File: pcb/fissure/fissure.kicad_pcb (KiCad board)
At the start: 2 copper layers, 213.5 x 98.2 mm, 64 parts, among them J1 Conn_01x04_Female, J2 USB_C_Receptacle_USB2.0, J3 Conn_01x06, J4 Conn_01x06, J5 OLED, J6 Conn_01x06, J7 Conn_01x06, K1 KEY, K10 KEY, K11 KEY, K12 KEY, K13 KEY, K14 KEY, K15 KEY, K16 KEY, K17 KEY, K18 KEY, K19 KEY, K2 KEY, K20 KEY, K3 KEY, K4 KEY, K5 KEY, K6 KEY, K7 KEY, K8 KEY, K9 KEY, Q1 AO3401A, Q2 AO3401A, SW1 SW_Push, SW2 SW_Push, SW3 SW_SPDT, SW4 SW_SPDT, U1 Holyiot_18010, U2 MT25QL128ABA1ESE, U3 LTC4054ES5-4.2, U4 MCP1700-3302E_SOT23

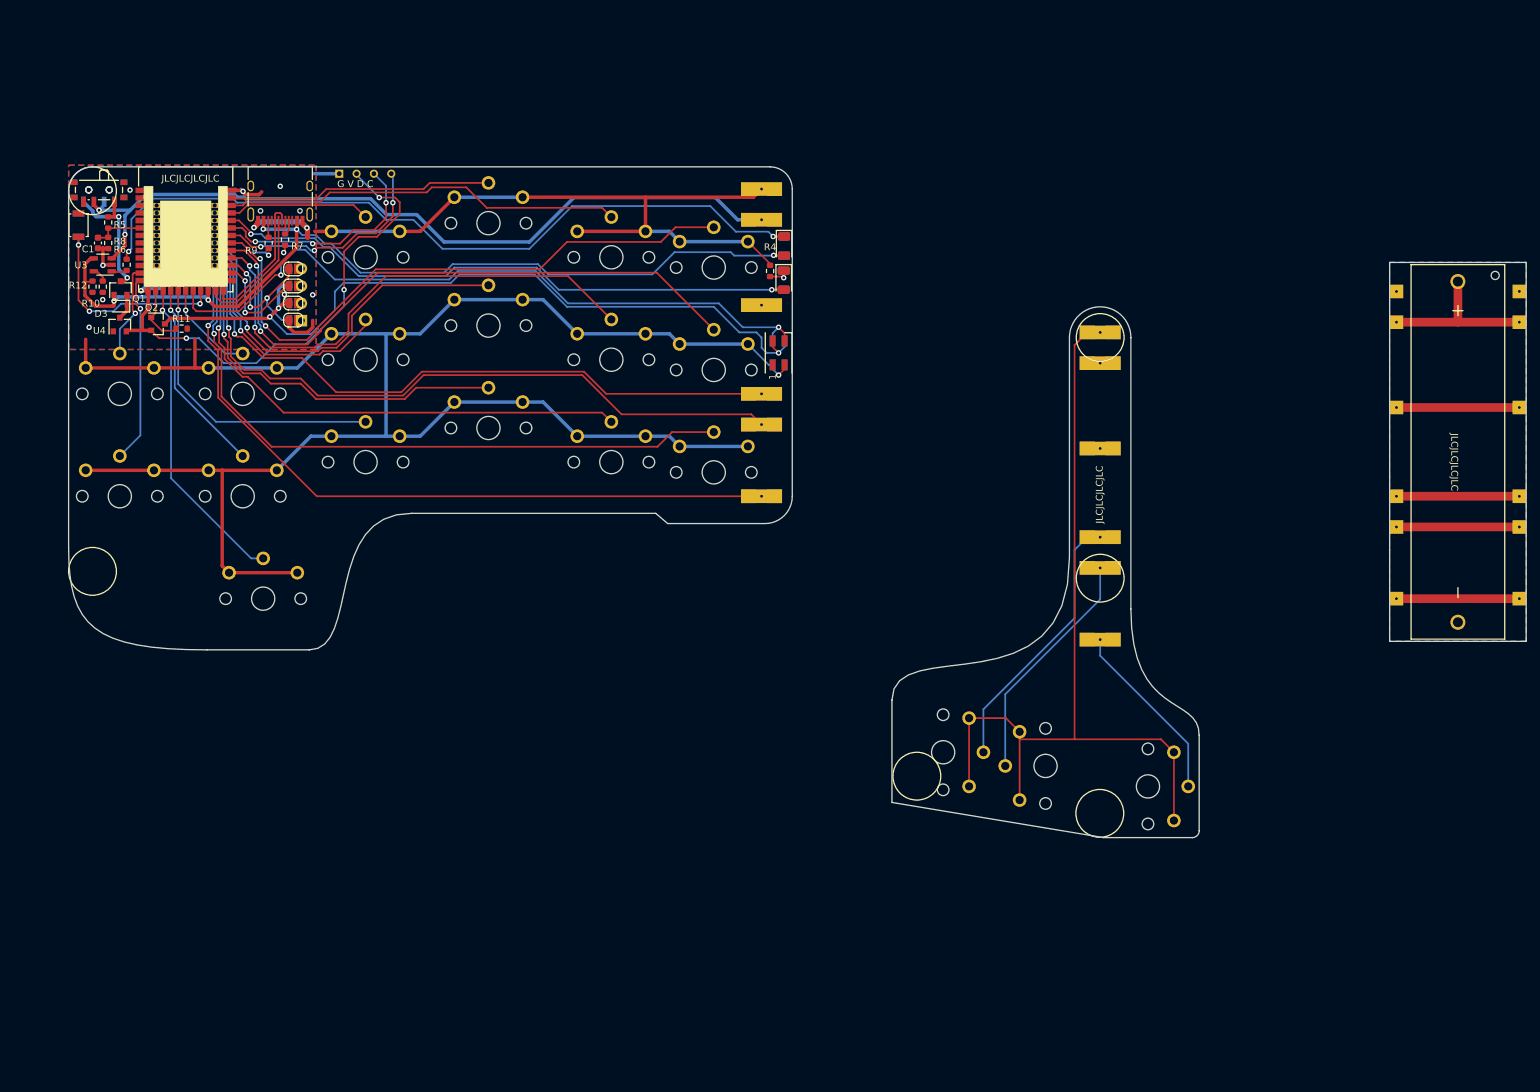
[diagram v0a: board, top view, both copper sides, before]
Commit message: stagger update
- middle 2 mm up
- outer index flat with home
- narrower pinky columns
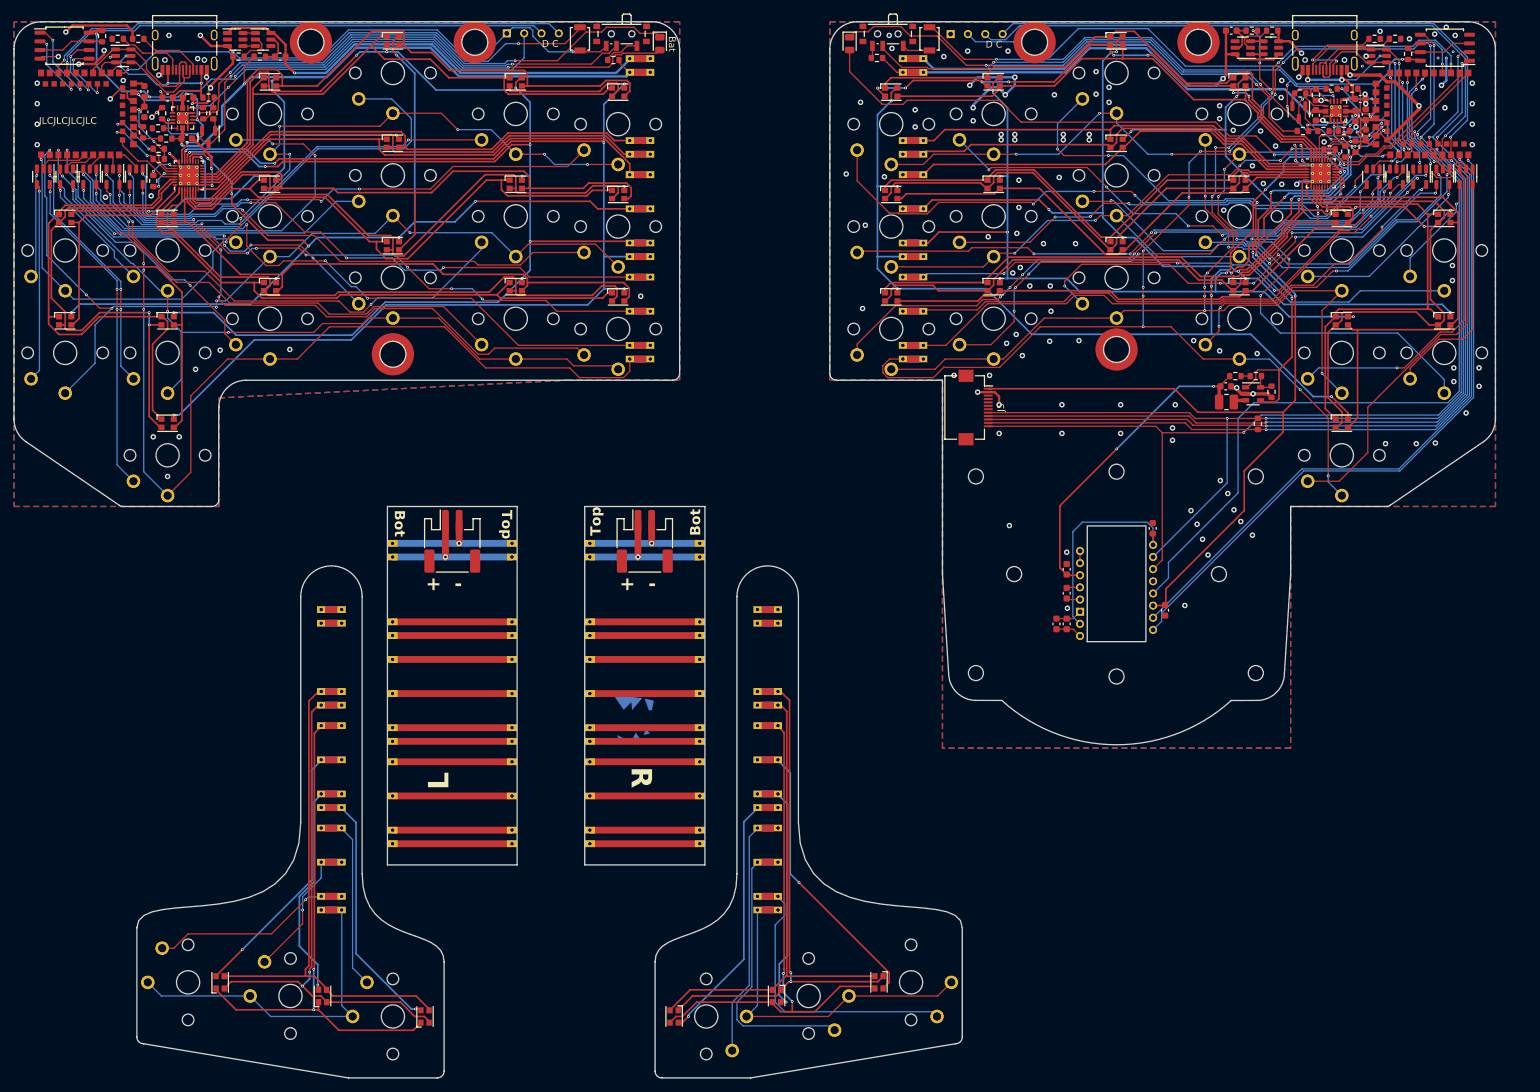
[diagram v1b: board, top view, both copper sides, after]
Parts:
- removed D41, D42: SK6812MINI, LED_SMD:LED_SK6812MINI_PLCC4_3.5x3.5mm_P1.75mm
- removed JP1, JP2, JP3, JP4, JP5, JP6, JP7, JP8: SolderJumper_2_Open, Jumper:SolderJumper-2_P1.3mm_Open_RoundedPad1.0x1.5mm
- added ?: , soldered-nuts:M2, F.Cu at (191.5, 38.0)
- added ?: , soldered-nuts:M2, F.Cu at (167.5, 38.0)
- added ?: , soldered-nuts:M2, F.Cu at (73.5, 83.7)
- added ?: , soldered-nuts:M2, F.Cu at (61.5, 38.0)
- added ?: , soldered-nuts:M2, F.Cu at (179.5, 83.0)
- added ?: , soldered-nuts:M2, F.Cu at (85.5, 38.0)
- added BT2: Battery_Cell, Connector_JST:JST_PH_S2B-PH-SM4-TB_1x02-1MP_P2.00mm_Horizontal, F.Cu at (110.4, 111.1)
- added C10: 10uF, Capacitor_SMD:C_0603_1608Metric, F.Cu at (170.7, 123.2)
- added C11: 10nF, Capacitor_SMD:C_0603_1608Metric, F.Cu at (172.2, 123.2)
- added C12: 10uF, Capacitor_SMD:C_0603_1608Metric, F.Cu at (195.5, 88.4)
- added C13: 4.7uF, Capacitor_SMD:C_0603_1608Metric, F.Cu at (215.2, 46.3)
- added C14: 4.7uF, Capacitor_SMD:C_0603_1608Metric, F.Cu at (214.5, 48.8)
- added C15: 4.7uF, Capacitor_SMD:C_0603_1608Metric, F.Cu at (208.7, 48.7)
- added C16: 0.1uF, Capacitor_SMD:C_0603_1608Metric, F.Cu at (57.0, 40.1)
- added C17: 0.1uF, Capacitor_SMD:C_0603_1608Metric, F.Cu at (196.3, 36.3)
- added C2: 4.7uF, Capacitor_SMD:C_0603_1608Metric, F.Cu at (40.5, 46.1)
- added C3: 4.7uF, Capacitor_SMD:C_0603_1608Metric, F.Cu at (43.5, 46.1)
- added C4: 4.7uF, Capacitor_SMD:C_0603_1608Metric, F.Cu at (43.3, 52.1)
- added C5: 4.7uF, Capacitor_SMD:C_0603_1608Metric, F.Cu at (216.0, 48.6)
- added C6: 100nF, Capacitor_SMD:C_0603_1608Metric, F.Cu at (186.6, 121.2)
- added C7: 100nF, Capacitor_SMD:C_0603_1608Metric, F.Cu at (172.2, 115.2)
- added C8: 100nF, Capacitor_SMD:C_0603_1608Metric, F.Cu at (172.2, 118.7)
- added C9: 10nF, Capacitor_SMD:C_0603_1608Metric, F.Cu at (184.8, 109.2)
- added D10: ~, Package_TO_SOT_SMD:SOT-23-5, F.Cu at (217.1, 57.7)
- added D11: ~, Package_TO_SOT_SMD:SOT-23-5, F.Cu at (230.7, 57.7)
- added D12: ~, Package_TO_SOT_SMD:SOT-23-5, F.Cu at (227.3, 57.7)
- added D6: ~, Package_TO_SOT_SMD:SOT-23-5, F.Cu at (32.5, 57.7)
- added D7: ~, Package_TO_SOT_SMD:SOT-23-5, F.Cu at (35.9, 57.7)
- added D8: ~, Package_TO_SOT_SMD:SOT-23-5, F.Cu at (223.9, 57.7)
- added D9: ~, Package_TO_SOT_SMD:SOT-23-5, F.Cu at (220.5, 57.7)
- added G***: LOGO, LOGO, B.Cu at (110.6, 136.0)
- added J11: Conn_01x12_Socket, fissure:bridge, B.Cu at (119.2, 130.1)
- added J12: Conn_01x12_Pin, fissure:bridge-conn, B.Cu at (149.7, 65.0)
- added J16: Conn_01x12_Pin, fissure:bridge-conn, F.Cu at (128.4, 145.7)
- added J17: Conn_01x12_Socket, fissure:bridge, F.Cu at (101.6, 130.1)
- added J8: USB_C_Receptacle_USB2.0, Connector_USB:USB_C_Receptacle_HRO_TYPE-C-31-M-12, F.Cu at (210.0, 38.0)
- added J9: debug-port, misc:debug-port-single-side, F.Cu at (159.0, 36.8)
- added K21: diode-choc, pg1350:pg1350-SR, F.Cu at (146.5, 50.0)
- added K22: diode-choc, pg1350:pg1350-SL, F.Cu at (161.5, 48.5)
- added K23: diode-choc, pg1350:pg1350-S, F.Cu at (179.5, 42.5)
- added K24: diode-choc, pg1350:pg1350-SR, F.Cu at (197.5, 48.5)
- added K25: diode-choc, pg1350:pg1350-SN, F.Cu at (212.5, 68.5)
- added K26: diode-choc, pg1350:pg1350-SR, F.Cu at (146.5, 65.0)
- added K27: diode-choc, pg1350:pg1350-SL, F.Cu at (161.5, 63.5)
- added K28: diode-choc, pg1350:pg1350-S, F.Cu at (179.5, 57.5)
- added K29: diode-choc, pg1350:pg1350-SR, F.Cu at (197.5, 63.5)
- added K30: diode-choc, pg1350:pg1350-SN, F.Cu at (212.5, 83.5)
- added K31: diode-choc, pg1350:pg1350-SR, F.Cu at (146.5, 80.0)
- added K32: diode-choc, pg1350:pg1350-SL, F.Cu at (161.5, 78.5)
- added K33: diode-choc, pg1350:pg1350-S, F.Cu at (179.5, 72.5)
- added K34: diode-choc, pg1350:pg1350-SR, F.Cu at (197.5, 78.5)
- added K35: diode-choc, pg1350:pg1350-SN, F.Cu at (212.5, 98.5)
- added K36: diode-choc, pg1350:pg1350-SN, F.Cu at (227.5, 68.5)
- added K37: diode-choc, pg1350:pg1350-SN, F.Cu at (227.5, 83.5)
- added K38: diode-choc, pg1350:pg1350-S, F.Cu at (119.4, 180.7)
- added K39: diode-choc, pg1350:pg1350-S, F.Cu at (134.4, 177.7)
- added K40: diode-choc, pg1350:pg1350-S, F.Cu at (149.4, 175.7)
- added L1: 10uH, Inductor_SMD:L_0603_1608Metric, F.Cu at (216.0, 51.6)
- added L2: 2.2uH, Inductor_SMD:L_1008_2520Metric, F.Cu at (195.6, 90.7)
- added L3: 10uH, Inductor_SMD:L_0603_1608Metric, F.Cu at (37.1, 45.2)
- added LED1: LED_BGRA, LED_SMD:LED_ASMB-KTF0-0A306, F.Cu at (40.5, 63.8)
- added LED10: LED_BGRA, LED_SMD:LED_ASMB-KTF0-0A306, F.Cu at (106.5, 60.3)
- added LED11: LED_BGRA, LED_SMD:LED_ASMB-KTF0-0A306, F.Cu at (40.5, 93.8)
- added LED12: LED_BGRA, LED_SMD:LED_ASMB-KTF0-0A306, F.Cu at (55.5, 73.8)
- added LED13: LED_BGRA, LED_SMD:LED_ASMB-KTF0-0A306, F.Cu at (73.5, 67.8)
- added LED14: LED_BGRA, LED_SMD:LED_ASMB-KTF0-0A306, F.Cu at (91.5, 73.8)
- added LED15: LED_BGRA, LED_SMD:LED_ASMB-KTF0-0A306, F.Cu at (106.5, 75.3)
- added LED16: LED_BGRA, LED_SMD:LED_ASMB-KTF0-0A306, F.Cu at (25.5, 63.8)
- added LED17: LED_BGRA, LED_SMD:LED_ASMB-KTF0-0A306, F.Cu at (25.5, 78.8)
- added LED18: LED_BGRA, LED_SMD:LED_ASMB-KTF0-0A306, F.Cu at (78.2, 180.7)
- added LED19: LED_BGRA, LED_SMD:LED_ASMB-KTF0-0A306, F.Cu at (63.2, 177.7)
- added LED2: LED_BGRA, LED_SMD:LED_ASMB-KTF0-0A306, F.Cu at (55.5, 43.8)
- added LED20: LED_BGRA, LED_SMD:LED_ASMB-KTF0-0A306, F.Cu at (48.2, 175.7)
- added LED21: LED_BGRA, LED_SMD:LED_ASMB-KTF0-0A306, F.Cu at (146.5, 45.3)
- added LED22: LED_BGRA, LED_SMD:LED_ASMB-KTF0-0A306, F.Cu at (161.5, 43.8)
- added LED23: LED_BGRA, LED_SMD:LED_ASMB-KTF0-0A306, F.Cu at (179.5, 37.8)
- added LED24: LED_BGRA, LED_SMD:LED_ASMB-KTF0-0A306, F.Cu at (197.5, 43.8)
- added LED25: LED_BGRA, LED_SMD:LED_ASMB-KTF0-0A306, F.Cu at (212.5, 63.8)
- added LED26: LED_BGRA, LED_SMD:LED_ASMB-KTF0-0A306, F.Cu at (146.5, 60.3)
- added LED27: LED_BGRA, LED_SMD:LED_ASMB-KTF0-0A306, F.Cu at (161.5, 58.8)
- added LED28: LED_BGRA, LED_SMD:LED_ASMB-KTF0-0A306, F.Cu at (179.5, 52.8)
- added LED29: LED_BGRA, LED_SMD:LED_ASMB-KTF0-0A306, F.Cu at (197.5, 58.8)
- added LED3: LED_BGRA, LED_SMD:LED_ASMB-KTF0-0A306, F.Cu at (73.5, 37.8)
- added LED30: LED_BGRA, LED_SMD:LED_ASMB-KTF0-0A306, F.Cu at (212.5, 78.8)
- added LED31: LED_BGRA, LED_SMD:LED_ASMB-KTF0-0A306, F.Cu at (146.5, 75.3)
- added LED32: LED_BGRA, LED_SMD:LED_ASMB-KTF0-0A306, F.Cu at (161.5, 73.8)
- added LED33: LED_BGRA, LED_SMD:LED_ASMB-KTF0-0A306, F.Cu at (179.5, 67.8)
- added LED34: LED_BGRA, LED_SMD:LED_ASMB-KTF0-0A306, F.Cu at (197.5, 73.8)
- added LED35: LED_BGRA, LED_SMD:LED_ASMB-KTF0-0A306, F.Cu at (212.5, 93.8)
- added LED36: LED_BGRA, LED_SMD:LED_ASMB-KTF0-0A306, F.Cu at (227.5, 78.8)
- added LED37: LED_BGRA, LED_SMD:LED_ASMB-KTF0-0A306, F.Cu at (227.5, 63.8)
- added LED38: LED_BGRA, LED_SMD:LED_ASMB-KTF0-0A306, F.Cu at (114.7, 180.7)
- added LED39: LED_BGRA, LED_SMD:LED_ASMB-KTF0-0A306, F.Cu at (129.7, 177.7)
- added LED4: LED_BGRA, LED_SMD:LED_ASMB-KTF0-0A306, F.Cu at (91.5, 43.8)
- added LED40: LED_BGRA, LED_SMD:LED_ASMB-KTF0-0A306, F.Cu at (144.7, 175.7)
- added LED5: LED_BGRA, LED_SMD:LED_ASMB-KTF0-0A306, F.Cu at (106.5, 45.3)
- added LED6: LED_BGRA, LED_SMD:LED_ASMB-KTF0-0A306, F.Cu at (40.5, 78.8)
- added LED7: LED_BGRA, LED_SMD:LED_ASMB-KTF0-0A306, F.Cu at (55.5, 58.8)
- added LED8: LED_BGRA, LED_SMD:LED_ASMB-KTF0-0A306, F.Cu at (73.5, 52.8)
- added LED9: LED_BGRA, LED_SMD:LED_ASMB-KTF0-0A306, F.Cu at (91.5, 58.8)
- added R1: 10k, Resistor_SMD:R_0603_1608Metric, F.Cu at (39.1, 50.6)
- added R13: 5.1k, Resistor_SMD:R_0603_1608Metric, F.Cu at (217.3, 37.5)
- added R14: 5.1k, Resistor_SMD:R_0603_1608Metric, F.Cu at (220.3, 37.5)
- added R15: 10k, Resistor_SMD:R_0603_1608Metric, F.Cu at (206.4, 45.5)
- added R16: 10k, Resistor_SMD:R_0603_1608Metric, F.Cu at (208.7, 45.7)
- added R17: 1k, Resistor_SMD:R_0603_1608Metric, F.Cu at (206.8, 51.0)
- added R18: 100k, Resistor_SMD:R_0603_1608Metric, F.Cu at (211.0, 44.8)
- added R19: 100k, Resistor_SMD:R_0603_1608Metric, F.Cu at (214.0, 44.8)
- added R2: 10k, Resistor_SMD:R_0603_1608Metric, F.Cu at (39.7, 48.4)
- added R20: 100k, Resistor_SMD:R_0603_1608Metric, F.Cu at (222.2, 39.7)
- added R21: 100k, Resistor_SMD:R_0603_1608Metric, F.Cu at (105.8, 40.6)
- added R22: 10k, Resistor_SMD:R_0603_1608Metric, F.Cu at (38.4, 58.3)
- added R23: 10k, Resistor_SMD:R_0603_1608Metric, F.Cu at (210.7, 53.7)
- added R24: 100k, Resistor_SMD:R_0603_1608Metric, F.Cu at (144.4, 40.3)
- added R25: 100k, Resistor_SMD:R_0603_1608Metric, F.Cu at (46.5, 46.1)
- added R26: 100k, Resistor_SMD:R_0603_1608Metric, F.Cu at (212.8, 51.0)
- added R27: 1k, Resistor_SMD:R_0603_1608Metric, F.Cu at (47.2, 48.4)
- added R28: 1k, Resistor_SMD:R_0603_1608Metric, F.Cu at (209.8, 51.0)
- added R29: 5.1k, Resistor_SMD:R_0603_1608Metric, F.Cu at (39.2, 53.6)
- added R30: 5.1k, Resistor_SMD:R_0603_1608Metric, F.Cu at (39.2, 55.1)
- added R31: 100, Resistor_SMD:R_0603_1608Metric, F.Cu at (54.0, 40.1)
- added R32: 100, Resistor_SMD:R_0603_1608Metric, F.Cu at (199.3, 36.3)
- added R33: 1k, Resistor_SMD:R_0603_1608Metric, F.Cu at (50.9, 40.1)
- added R34: 1k, Resistor_SMD:R_0603_1608Metric, F.Cu at (202.3, 36.3)
- added R35: 5.1k, Resistor_SMD:R_0603_1608Metric, F.Cu at (213.0, 54.0)
- added R36: 5.1k, Resistor_SMD:R_0603_1608Metric, F.Cu at (214.5, 53.3)
- added REF**: MountingHole_2.2mm_M2_DIN965, MountingHole:MountingHole_2.2mm_M2_DIN965, F.Cu at (194.5, 115.9)
- added REF**: MountingHole_2.2mm_M2_DIN965, MountingHole:MountingHole_2.2mm_M2_DIN965, F.Cu at (164.5, 115.9)
- added REF**: nothing, misc:nothing, F.Cu at (105.5, 84.5)
- added REF**: MountingHole_2.2mm_M2_DIN965, MountingHole:MountingHole_2.2mm_M2_DIN965, F.Cu at (179.5, 100.9)
- added REF**: MountingHole_2.2mm_M2_DIN965, MountingHole:MountingHole_2.2mm_M2_DIN965, F.Cu at (179.5, 130.9)
- added REF**: MountingHole_2.2mm_M2_DIN965, MountingHole:MountingHole_2.2mm_M2_DIN965, F.Cu at (158.9, 101.6)
- added REF**: embedded, misc:embedded, B.Cu at (84.0, 136.0)
- added REF**: crides-neg, misc:crides-neg, B.Cu at (84.0, 150.5)
- added REF**4: MountingHole_2.2mm_M2_DIN965, MountingHole:MountingHole_2.2mm_M2_DIN965, F.Cu at (199.9, 101.6)
- added REF**5: MountingHole_2.2mm_M2_DIN965, MountingHole:MountingHole_2.2mm_M2_DIN965, F.Cu at (158.9, 130.4)
- added REF**6: MountingHole_2.2mm_M2_DIN965, MountingHole:MountingHole_2.2mm_M2_DIN965, F.Cu at (199.9, 130.4)
- added U10: W25Q128JVS, Package_SO:SOIC-8_5.23x5.23mm_P1.27mm, F.Cu at (227.6, 38.8)
- added U11: DW01A, Package_TO_SOT_SMD:SOT-23-6, F.Cu at (54.5, 37.6)
- added U12: e73-2gm08s1c, mcu:e73-2g4m08s1c-shrunk, F.Cu at (27.0, 48.5)
- added U13: IS31FL3729, Package_DFN_QFN:QFN-32-1EP_4x4mm_P0.4mm_EP2.9x2.9mm_ThermalVias, F.Cu at (209.4, 57.2)
- added U14: DW01A, Package_TO_SOT_SMD:SOT-23-6, F.Cu at (198.0, 38.8)
- added U15: FS8205, Package_TO_SOT_SMD:SOT-23-6, F.Cu at (50.4, 37.6)
- added U16: FS8205, Package_TO_SOT_SMD:SOT-23-6, F.Cu at (202.1, 38.8)
- added U5: PMW3610, sensor:PMW3610, B.Cu at (179.5, 115.9)
- added U6: IS31FL3729, Package_DFN_QFN:QFN-32-1EP_4x4mm_P0.4mm_EP2.9x2.9mm_ThermalVias, F.Cu at (43.6, 57.5)
- added U7: SRV05-4, Package_TO_SOT_SMD:SOT-23-6, F.Cu at (217.9, 40.0)
- added U8: SRV05-4, Package_TO_SOT_SMD:SOT-23-6, F.Cu at (34.0, 40.0)
- added U9: BQ24075, Package_DFN_QFN:VQFN-16-1EP_3x3mm_P0.5mm_EP1.68x1.68mm_ThermalVias, F.Cu at (211.6, 48.1)
- BT1: footprint misc:BA1AAAPC -> Connector_JST:JST_PH_S2B-PH-SM4-TB_1x02-1MP_P2.00mm_Horizontal
- C1: value 10nF -> 4.7uF
- D1: value BLUE -> RED; footprint LED_SMD:LED_1206_3216Metric -> LED_SMD:LED_0805_2012Metric
- D2: footprint LED_SMD:LED_1206_3216Metric -> LED_SMD:LED_0805_2012Metric; moved to F.Cu
- D3: value 1N5819 -> ~; footprint Diode_SMD:D_SOD-323 -> Package_TO_SOT_SMD:SOT-23-5
- D4: value BLUE -> ~; footprint LED_SMD:LED_1206_3216Metric -> Package_TO_SOT_SMD:SOT-23-5; moved to F.Cu
- D5: value RED -> ~; footprint LED_SMD:LED_1206_3216Metric -> Package_TO_SOT_SMD:SOT-23-5
- J1: value Conn_01x04_Female -> debug-port; footprint fissure:debug-port -> misc:debug-port-single-side
- J3: value Conn_01x06 -> Conn_01x12_Pin; moved to B.Cu
- J4: value Conn_01x06 -> Conn_01x12_Pin; moved to F.Cu
- J5: value OLED -> cirque-trackpad; footprint misc:OLED -> Connector_FFC-FPC:Hirose_FH12-12S-0.5SH_1x12-1MP_P0.50mm_Horizontal; moved to F.Cu
- J6: value Conn_01x06 -> Conn_01x12_Socket
- J7: value Conn_01x06 -> Conn_01x12_Socket; moved to B.Cu
- K1, K11, K16, K17, K6: value KEY -> diode-choc; footprint pg1350:PG1350-reversible-no-diode-short -> pg1350:pg1350-SN
- K10, K15, K5: value KEY -> diode-choc; footprint pg1350:PG1350-reversible-no-diode-short-offcenter-outer -> pg1350:pg1350-SL
- K12, K2, K7: value KEY -> diode-choc; footprint pg1350:PG1350-reversible-no-diode-short -> pg1350:pg1350-SL
- K13, K18, K19, K20, K3, K8: value KEY -> diode-choc; footprint pg1350:PG1350-reversible-no-diode-short -> pg1350:pg1350-S
- K14, K4, K9: value KEY -> diode-choc; footprint pg1350:PG1350-reversible-no-diode-short-offcenter -> pg1350:pg1350-SR
- Q1, Q2: value AO3401A -> AO3400A
- R10: value 10k -> 100k
- R11: value 2M -> 100k
- R3: value 10k -> 100k; footprint Resistor_SMD:R_0805_2012Metric -> Resistor_SMD:R_0603_1608Metric; moved to F.Cu
- R4: value 1k -> 10k
- R5, R8: value 5.1M -> 100k
- SW2, SW3: moved to F.Cu
- U1: value Holyiot_18010 -> e73-2gm08s1c; footprint misc:Holyiot_18010 -> mcu:e73-2g4m08s1c-shrunk
- U2: value MT25QL128ABA1ESE -> W25Q128JVS; footprint Package_SO:SOP-8_5.28x5.23mm_P1.27mm -> Package_SO:SOIC-8_5.23x5.23mm_P1.27mm; moved to F.Cu
- U3: value LTC4054ES5-4.2 -> BQ24075; footprint Package_TO_SOT_SMD:TSOT-23-5 -> Package_DFN_QFN:VQFN-16-1EP_3x3mm_P0.5mm_EP1.68x1.68mm_ThermalVias
- U4: value MCP1700-3302E_SOT23 -> TLV62568DBV; footprint Package_TO_SOT_SMD:SOT-23 -> Package_TO_SOT_SMD:SOT-23-5
- moved U1 183.6 mm to (226.0, 48.5), turned to -90 degrees
- moved R12 173.4 mm to (202.2, 89.2), turned to 90 degrees
- moved Q2 169.9 mm to (206.2, 48.3), turned to -90 degrees
- moved R10 166.4 mm to (196.9, 86.9), turned to 0 degrees
- moved U4 166.3 mm to (199.5, 89.5), turned to 0 degrees
- moved R11 157.5 mm to (199.9, 86.9)
- moved J6 150.9 mm to (72.7, 130.1), turned to -90 degrees
- moved J7 150.0 mm to (91.7, 130.1), turned to -90 degrees
- moved BT1 147.9 mm to (82.2, 111.1), turned to 0 degrees
- moved SW2 127.6 mm to (152.1, 37.5), turned to -90 degrees
- moved J4 119.6 mm to (64.5, 145.7)
- moved SW3 117.8 mm to (146.0, 37.1), turned to 180 degrees
- moved K18 115.6 mm to (73.5, 180.7), turned to 90 degrees
- moved K19 115.6 mm to (58.5, 177.7)
- moved K20 115.6 mm to (43.5, 175.7), turned to 90 degrees
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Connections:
- BT1 pad 1: bridge_BAT -> Net-(BT1-+)
- BT1 pad 2: bridge_GND -> Net-(BT1--)
- C1 pad 1: BAT_MEAS -> L_3V3
- C1 pad 2: GND -> L_GND
- D1 pad 1: Net-(D1-Pad1) -> Net-(D1-K)
- D1 pad 2: BLUE -> L_VDDH
- D2 pad 1: Net-(D2-Pad1) -> Net-(D2-K)
- D2 pad 2: VBUS -> R_VDDH
- D3 pad 1: Net-(D3-Pad1) -> Net-(D3A-A)
- D3 pad 2: VBUS -> L_COL0
- D4 pad 1: Net-(D1-Pad1) -> Net-(D4A-A)
- D4 pad 2: BLUE -> L_COL1
- D5 pad 1: Net-(D2-Pad1) -> Net-(D5A-A)
- D5 pad 2: VBUS -> L_COL2
- J1 pad 1: GND -> L_GND
- J1 pad 2: VDD -> L_3V3
- J1 pad 3: SWC -> L_SWD
- J1 pad 4: SWD -> L_SWC
- J2 pad A1: GND -> L_GND
- J2 pad A12: GND -> L_GND
- J2 pad A4: VBUS -> L_VBUS
- J2 pad A6: D+ -> L_D+
- J2 pad A7: D- -> L_D-
- J2 pad A9: VBUS -> L_VBUS
- J2 pad B1: GND -> L_GND
- J2 pad B12: GND -> L_GND
- J2 pad B4: VBUS -> L_VBUS
- J2 pad B6: D+ -> L_D+
- J2 pad B7: D- -> L_D-
- J2 pad B9: VBUS -> L_VBUS
- J3 pad 1: GND -> L_ROW3
- J3 pad 2: BAT -> Net-(D5D-A)
- J3 pad 3: unconnected-(J3-Pad3) -> Net-(D6D-A)
- J3 pad 4: K20 -> Net-(D7D-A)
- J3 pad 5: K19 -> /thumb+led_l/A3
- J3 pad 6: K18 -> /thumb+led_l/A2
- J4 pad 1: thumb_GND -> Net-(J4-Pin_1)
- J4 pad 2: thumb_BAT -> Net-(J4-Pin_2)
- J4 pad 3: unconnected-(J4-Pad3) -> Net-(J4-Pin_3)
- J4 pad 4: thumb_K20 -> Net-(J4-Pin_4)
- J4 pad 5: thumb_K19 -> /thumb+led_l/T_A3
- J4 pad 6: thumb_K18 -> /thumb+led_l/T_A2
- J5 pad 1: Net-(J5-Pad1) -> R_3V3
- J5 pad 2: Net-(J5-Pad2) -> L_GND
- J5 pad 3: Net-(J5-Pad3) -> unconnected-(J5-SDA-Pad3)
- J5 pad 4: Net-(J5-Pad4) -> unconnected-(J5-SCL-Pad4)
- J6 pad 1: bridge_GND -> Net-(J6-Pin_1)
- J6 pad 2: bridge_BAT -> Net-(J6-Pin_2)
- J7 pad 1: bridge_GND -> Net-(J6-Pin_1)
- J7 pad 2: bridge_BAT -> Net-(J6-Pin_2)
- K1 pad 1: K1 -> L_ROW2
- K1 pad 2: GND -> Net-(D4C-A)
- K10 pad 1: K10 -> L_ROW1
- K10 pad 2: GND -> Net-(D7B-A)
- K11 pad 1: K11 -> L_ROW3
- K11 pad 2: GND -> Net-(D3D-A)
- K12 pad 1: K12 -> L_ROW3
- K12 pad 2: GND -> Net-(D4D-A)
- K13 pad 1: K13 -> L_ROW2
- K13 pad 2: GND -> Net-(D5C-A)
- K14 pad 1: K14 -> L_ROW2
- K14 pad 2: GND -> Net-(D6C-A)
- K15 pad 1: K15 -> L_ROW2
- K15 pad 2: GND -> Net-(D7C-A)
- K16 pad 1: K16 -> L_ROW0
- K16 pad 2: GND -> Net-(D3B-A)
- K17 pad 1: K17 -> L_ROW1
- K17 pad 2: GND -> Net-(D3C-A)
- K18 pad 1: thumb_K18 -> Net-(J4-Pin_1)
- K18 pad 2: thumb_GND -> Net-(J4-Pin_4)
- K19 pad 1: thumb_K19 -> Net-(J4-Pin_1)
- K19 pad 2: thumb_GND -> Net-(J4-Pin_3)
- K2 pad 1: K2 -> L_ROW0
- K2 pad 2: GND -> Net-(D4A-A)
- K20 pad 1: thumb_K20 -> Net-(J4-Pin_1)
- K20 pad 2: thumb_GND -> Net-(J4-Pin_2)
- K3 pad 1: K3 -> L_ROW0
- K3 pad 2: GND -> Net-(D5A-A)
- K4 pad 1: K4 -> L_ROW0
- K4 pad 2: GND -> Net-(D6A-A)
- K5 pad 1: K5 -> L_ROW0
- K5 pad 2: GND -> Net-(D7A-A)
- K6 pad 1: K6 -> L_ROW2
- K6 pad 2: GND -> Net-(D3A-A)
- K7 pad 1: K7 -> L_ROW1
- K7 pad 2: GND -> Net-(D4B-A)
- K8 pad 1: K8 -> L_ROW1
- K8 pad 2: GND -> Net-(D5B-A)
- K9 pad 1: K9 -> L_ROW1
- K9 pad 2: GND -> Net-(D6B-A)
- Q1 pad 1: VBUS -> Net-(Q1-G)
- Q1 pad 2: Net-(D3-Pad1) -> L_GND
- Q1 pad 3: MCU_BAT -> /power_l/SYSOFF
- Q2 pad 1: VCC_SWITCH -> Net-(Q2-G)
- Q2 pad 2: VDD -> L_GND
- Q2 pad 3: EXT_VCC -> /power_r/SYSOFF
- R10 pad 1: Net-(R10-Pad1) -> +1V8
- R10 pad 2: GND -> Net-(R10-Pad2)
- R11 pad 1: VCC_SWITCH -> Net-(R10-Pad2)
- R11 pad 2: GND -> Net-(U4-FB)
- R12 pad 1: VBUS -> L_GND
- R12 pad 2: GND -> Net-(U4-FB)
- R3 pad 1: VDD -> Net-(U2-IO2)
- R3 pad 2: Net-(R3-Pad2) -> L_3V3
- R4 pad 1: Net-(D1-Pad1) -> R_MOSI
- R4 pad 2: GND -> R_MISO
- R5 pad 1: MCU_BAT -> L_BAT+
- R5 pad 2: BAT_MEAS -> L_BAT_MEAS
- R6 pad 1: Net-(D2-Pad1) -> Net-(U3-~{CHG})
- R6 pad 2: Net-(R6-Pad2) -> Net-(D1-K)
- R7 pad 1: GND -> L_GND
- R8 pad 1: BAT_MEAS -> L_BAT_MEAS
- R8 pad 2: GND -> L_BAT_MEAS_EN
- R9 pad 1: GND -> L_GND
- SW1 pad 1: RST -> L_RST
- SW1 pad 2: GND -> L_GND
- SW2 pad 1: RST -> R_RST
- SW2 pad 2: GND -> L_GND
- SW3 pad 1: MCU_BAT -> L_GND
- SW3 pad 2: BAT -> /power_r/SYSOFF
- SW3 pad 3: unconnected-(SW3-Pad3) -> /power_r/BAT_PULLUP
- SW4 pad 1: MCU_BAT -> /power_l/BAT_PULLUP
- SW4 pad 2: BAT -> /power_l/SYSOFF
- SW4 pad 3: unconnected-(SW4-Pad3) -> L_GND
- U1 pad 1: GND -> R_ROW0
- U1 pad 10: unconnected-(U1-Pad10) -> R_COL4
- U1 pad 12: K16 -> unconnected-(U1-P0.26-Pad12)
- U1 pad 13: K17 -> unconnected-(U1-XL2_P0.01-Pad13)
- U1 pad 15: unconnected-(U1-Pad15) -> R_BAT_MEAS
- U1 pad 16: CS -> unconnected-(U1-P0.08-Pad16)
- U1 pad 17: unconnected-(U1-Pad17) -> R_BAT_MEAS_EN
- U1 pad 18: MISO_DQ1 -> R_LED_SHDN
- U1 pad 19: unconnected-(U1-Pad19) -> R_3V3
- U1 pad 2: unconnected-(U1-Pad2) -> R_ROW1
- U1 pad 20: MOSI_DQ0 -> R_SCL
- U1 pad 21: unconnected-(U1-Pad21) -> L_GND
- U1 pad 22: SCLK -> R_SDA
- U1 pad 23: unconnected-(U1-Pad23) -> R_VDDH
- U1 pad 24: K18 -> L_GND
- U1 pad 25: K15 -> Net-(U1-DCCH)
- U1 pad 26: K14 -> R_RST
- U1 pad 27: K13 -> R_VBUS
- U1 pad 28: K8 -> MOUSE_~{CS}
- U1 pad 29: K7 -> R_D-
- U1 pad 3: unconnected-(U1-Pad3) -> R_ROW2
- U1 pad 30: K20 -> R_SCLK
- U1 pad 31: K19 -> R_D+
- U1 pad 32: GND -> R_MOSI
- U1 pad 33: K3 -> TP_DR
- U1 pad 34: K4 -> R_MISO
- U1 pad 35: K2 -> TP_~{CS}
- U1 pad 36: BLUE -> R_CS
- U1 pad 37: SWC -> R_SWD
- U1 pad 38: SWD -> unconnected-(U1-[L]_P1.02-Pad38)
- U1 pad 39: K5 -> R_SWC
- U1 pad 4: unconnected-(U1-Pad4) -> R_ROW3
- U1 pad 40: K10 -> unconnected-(U1-[L]_P1.04-Pad40)
- U1 pad 41: K9 -> MOUSE_~{RST}
- U1 pad 42: SDA -> unconnected-(U1-[L]_P1.06-Pad42)
- U1 pad 43: SCL -> MOTION
- U1 pad 5: unconnected-(U1-Pad5) -> L_GND
- U1 pad 6: BAT_MEAS -> R_COL0
- U1 pad 7: unconnected-(U1-Pad7) -> R_COL1
- U1 pad 8: unconnected-(U1-Pad8) -> R_COL2
- U1 pad 9: unconnected-(U1-Pad9) -> R_COL3
- U2 pad 1: CS -> L_CS
- U2 pad 2: MISO_DQ1 -> L_MISO
- U2 pad 3: Net-(R3-Pad2) -> Net-(U2-IO2)
- U2 pad 4: GND -> L_GND
- U2 pad 5: MOSI_DQ0 -> L_MOSI
- U2 pad 6: SCLK -> L_SCLK
- U2 pad 7: Net-(R3-Pad2) -> Net-(U2-IO2)
- U2 pad 8: VDD -> L_3V3
- U3 pad 1: Net-(R6-Pad2) -> Net-(U3-TS)
- U3 pad 2: GND -> L_BAT+
- U3 pad 3: BAT -> L_BAT+
- U3 pad 4: VBUS -> L_GND
- U3 pad 5: Net-(R10-Pad1) -> L_GND
- U4 pad 1: GND -> R_VDDH
- U4 pad 2: VDD -> L_GND
- U4 pad 3: Net-(D3-Pad1) -> Net-(U4-SW)
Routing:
- net GND: track 404.5 -> 0.00 mm, vias 15 -> 0
- net L_GND: track 0.00 -> 249.2 mm, vias 0 -> 168
- net R_3V3: track 0.00 -> 221.5 mm, vias 0 -> 8
- net /thumb+led_l/A3: track 0.00 -> 179.4 mm, vias 0 -> 7
- net R_ROW3: track 0.00 -> 168.8 mm, vias 0 -> 12
- net R_ROW0: track 0.00 -> 163.9 mm, vias 0 -> 9
- net R_ROW2: track 0.00 -> 162.9 mm, vias 0 -> 11
- net R_VDDH: track 0.00 -> 159.8 mm, vias 0 -> 7
- net /thumb+led_l/A2: track 0.00 -> 158.4 mm, vias 0 -> 8
- net /thumb+led_r/A3: track 0.00 -> 154.5 mm, vias 0 -> 9
- net R_MOSI: track 0.00 -> 154.5 mm, vias 0 -> 4
- net R_ROW1: track 0.00 -> 151.3 mm, vias 0 -> 6
- net R_SCLK: track 0.00 -> 150.2 mm, vias 0 -> 3
- net L_ROW3: track 0.00 -> 148.0 mm, vias 0 -> 5
- net /thumb+led_l/A1: track 0.00 -> 145.4 mm, vias 0 -> 8
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- added copper zone on B.Cu, net L_GND
- added copper zone on F.Cu, net L_GND
- removed copper zone on B.Cu, net GND
- removed copper zone on F.Cu, net GND
- removed copper zone on B.Cu, net bridge_GND
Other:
- board size 213.5 x 98.2 mm -> 217 x 154.7 mm
- board text added: "+ -"
- board text added: "Bat"
- board text added: "Bot"
- board text added: "L"
- board text added: "R"
- board text added: "Top"
- board text added: "fissure v3.3"
- board text removed: "G V D C"

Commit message: pcb, case
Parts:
- removed the REF** at (194.5, 115.9)
- removed the REF** at (164.5, 115.9)
- removed the REF** at (179.5, 100.9)
- removed the REF** at (179.5, 130.9)
- removed REF**4, REF**5, REF**6: MountingHole_2.2mm_M2_DIN965, MountingHole:MountingHole_2.2mm_M2_DIN965
- added REF**: MountingHole_2.2mm_M2_DIN965, MountingHole:MountingHole_2.2mm_M2_DIN965, F.Cu at (200.6, 98.9)
- added REF**: MountingHole_2.2mm_M2_DIN965, MountingHole:MountingHole_2.2mm_M2_DIN965, F.Cu at (200.6, 121.9)
- added REF**: MountingHole_2.2mm_M2_DIN965, MountingHole:MountingHole_2.2mm_M2_DIN965, F.Cu at (169.4, 121.9)
- added REF**3: MountingHole_2.2mm_M2_DIN965, MountingHole:MountingHole_2.2mm_M2_DIN965, F.Cu at (196.6, 107.3)
- added REF**3: MountingHole_2.2mm_M2_DIN965, MountingHole:MountingHole_2.2mm_M2_DIN965, F.Cu at (176.5, 101.9)
- added REF**3: MountingHole_2.2mm_M2_DIN965, MountingHole:MountingHole_2.2mm_M2_DIN965, F.Cu at (181.9, 122.0)
- moved J5 15.2 mm to (174.1, 90.9)
- moved REF** 10.8 mm to (169.4, 98.9)
- moved J16 9.20 mm to (137.6, 145.7)
- moved C10 7.78 mm to (176.2, 117.7)
- moved C11 7.78 mm to (177.7, 117.7)
- moved C6 7.78 mm to (192.1, 115.7)
- moved C7 7.78 mm to (177.7, 109.7)
- moved C8 7.78 mm to (177.7, 113.2)
- moved C9 7.78 mm to (190.3, 103.7)
- moved U5 7.78 mm to (185.0, 110.4)
- moved J4 2.80 mm to (61.7, 145.7)
- moved R4 1.30 mm to (201.5, 93.9)
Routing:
- net R_MOSI: track 154.5 -> 131.6 mm
- net R_3V3: track 221.5 -> 199.0 mm
- net R_SCLK: track 150.2 -> 129.7 mm
- net R_MISO: track 129.9 -> 114.9 mm
- net TP_DR: track 111.9 -> 97.0 mm
- net TP_~{CS}: track 110.7 -> 95.8 mm
- net R_ROW3: track 168.8 -> 158.1 mm
- net +1V8: track 47.7 -> 37.2 mm
- net MOUSE_~{RST}: track 96.2 -> 88.4 mm
- net MOUSE_~{CS}: track 108.1 -> 100.3 mm
- net MOTION: track 97.6 -> 89.9 mm
- net L_GND: track 249.2 -> 254.5 mm, vias 168 -> 163
- net Net-(J16-Pin_1): track 48.2 -> 52.6 mm
- net /thumb+led_r/T_R4: track 76.4 -> 72.1 mm
- net Net-(J16-Pin_4): track 34.0 -> 37.8 mm
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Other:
- outline, holes or cut-outs redrawn

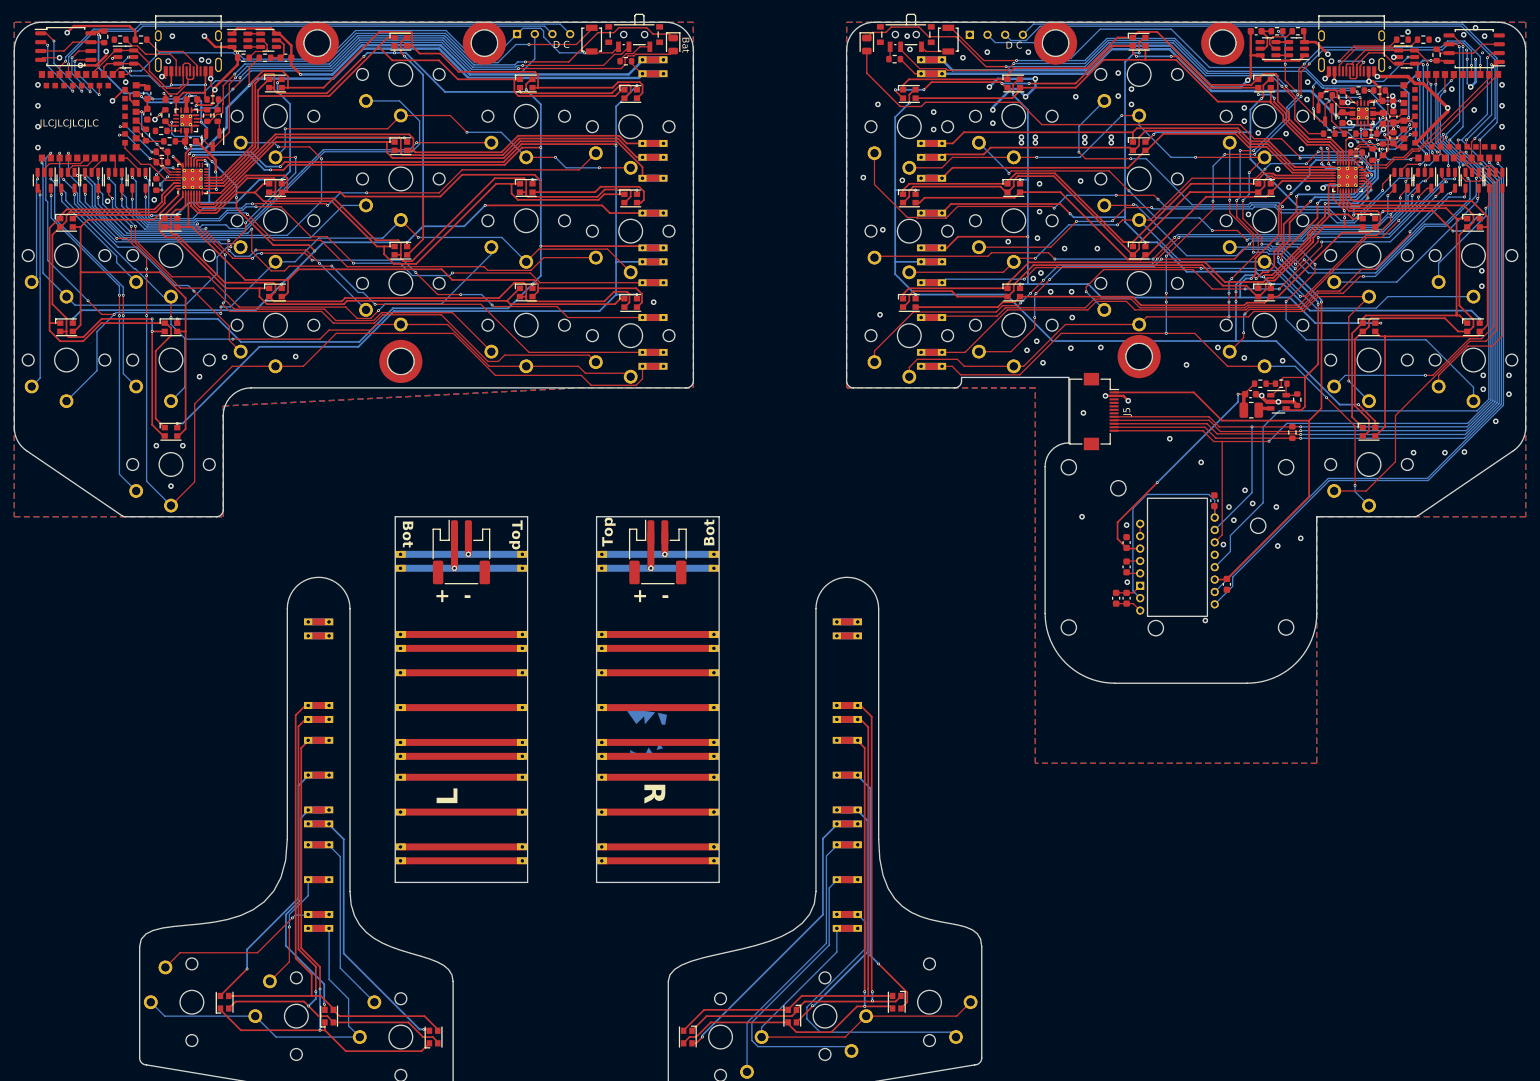
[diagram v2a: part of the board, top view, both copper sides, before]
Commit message: larger vias
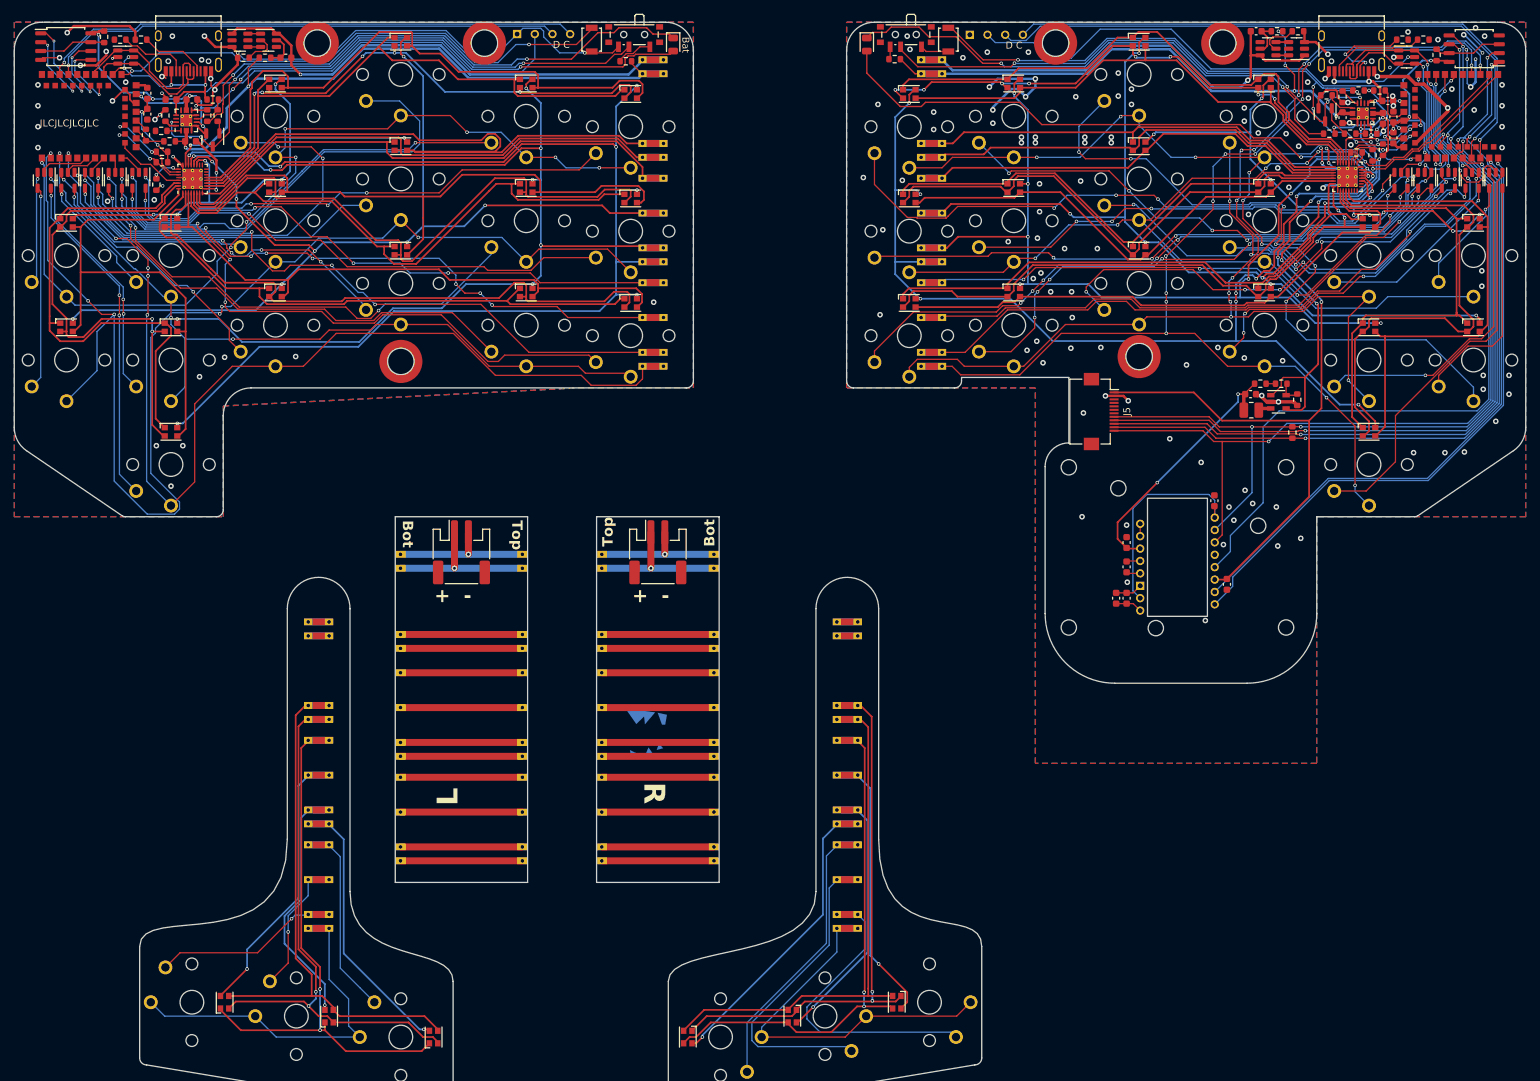
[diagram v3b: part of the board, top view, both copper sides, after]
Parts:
- moved R35 0.10 mm to (213.0, 54.1)
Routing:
- net L_ROW1: track 129.6 -> 187.9 mm
- net /thumb+led_l/R4: track 70.1 -> 95.6 mm
- net /thumb+led_l/G3: track 84.8 -> 80.6 mm, vias 3 -> 5
- net L_GND: track 254.5 -> 257.2 mm, vias 163 -> 162
- net TP_DR: track 97.0 -> 99.6 mm
- net R_COL3: track 16.1 -> 18.5 mm
- net Net-(D12C-A): track 55.1 -> 57.2 mm
- net R_ROW0: track 163.9 -> 165.8 mm
- net R_LED_SHDN: track 15.1 -> 16.9 mm
- net R_D+: track 30.4 -> 32.1 mm
- net R_D-: track 29.0 -> 30.6 mm
- net /thumb+led_r/A3: track 154.5 -> 156.2 mm
- net Net-(J8-CC1): track 14.7 -> 13.4 mm
- net R_VBUS: track 38.0 -> 38.9 mm
- net Net-(D5B-A): track 47.5 -> 48.4 mm
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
